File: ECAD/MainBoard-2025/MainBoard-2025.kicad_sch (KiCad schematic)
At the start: 60 parts, among them J1 XT60, J10 Conn_01x02, J11 Conn_01x04, J12 Conn_01x04, J15 Conn_01x02, J16 XT30, J17 XT30, J18 Conn_01x02, J2 Conn_01x04, J20 BAU, J21 BAU, J22 Conn_01x04, J23 Conn_01x02, J26 BAU, J28 Conn_01x02, J29 Conn_01x02, J3 ConStep1, J4 Conn_01x02, J5 ConStep1, J6 ConStep1, J7 XT30, J8 Conn_01x02, J9 Conn_01x02, K2 FINDER-36.11, U2 R-78B3.3-2.0, U3 R-78B12-2.0, U4 R-78B5.0-2.0, U5 Teensy4.1

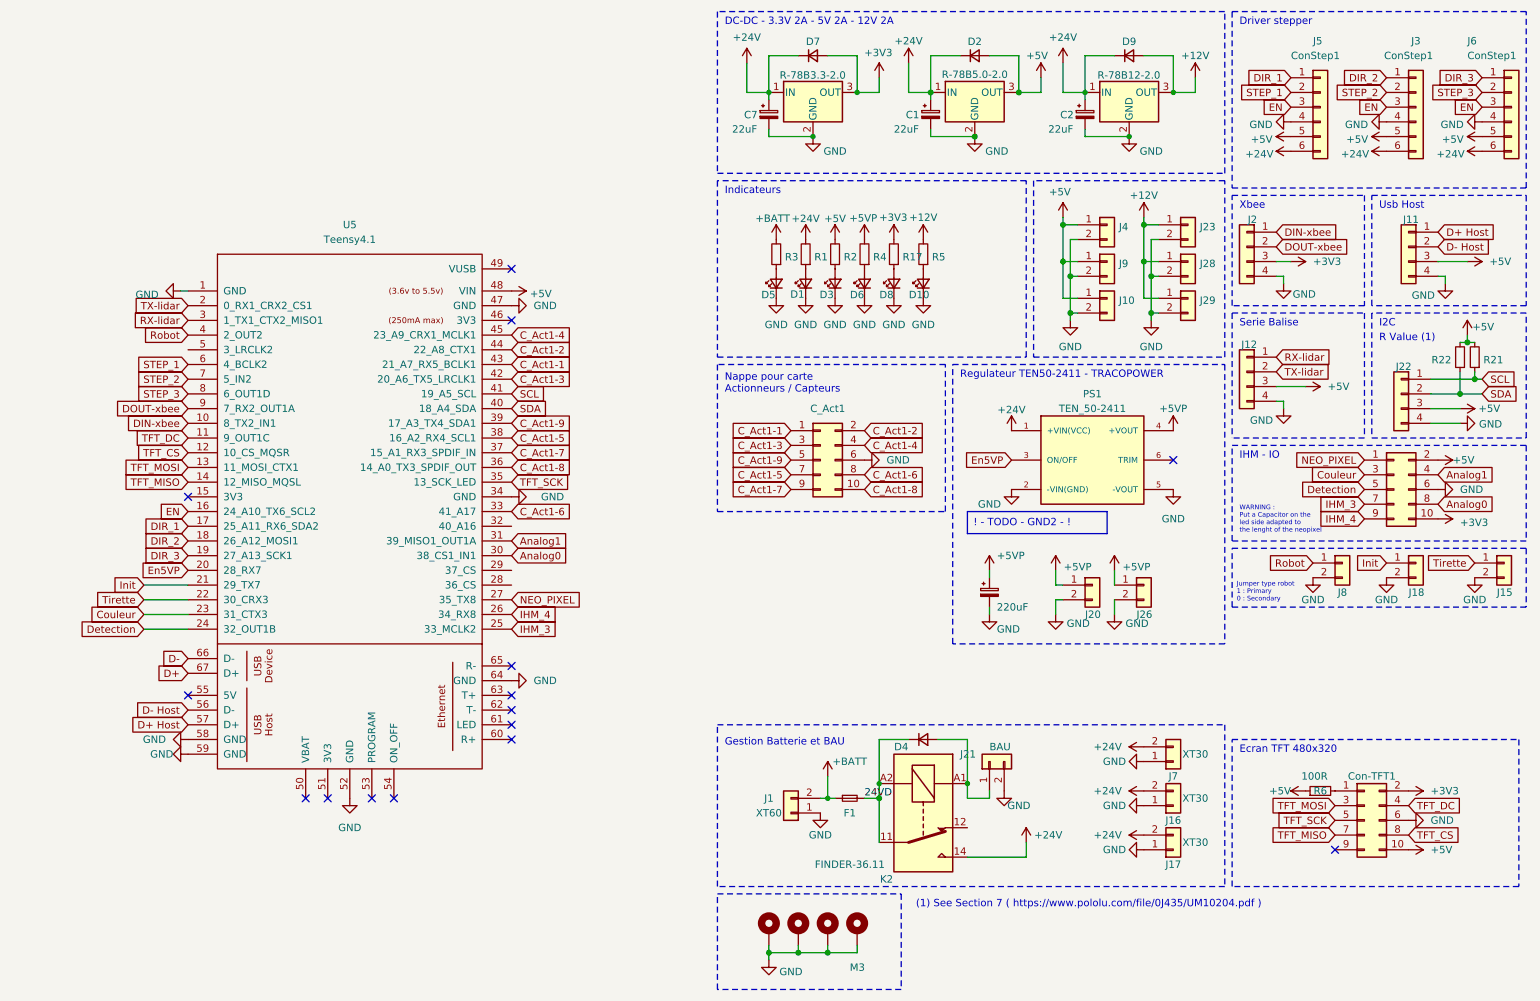
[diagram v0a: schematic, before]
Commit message: add buzzer and res on program
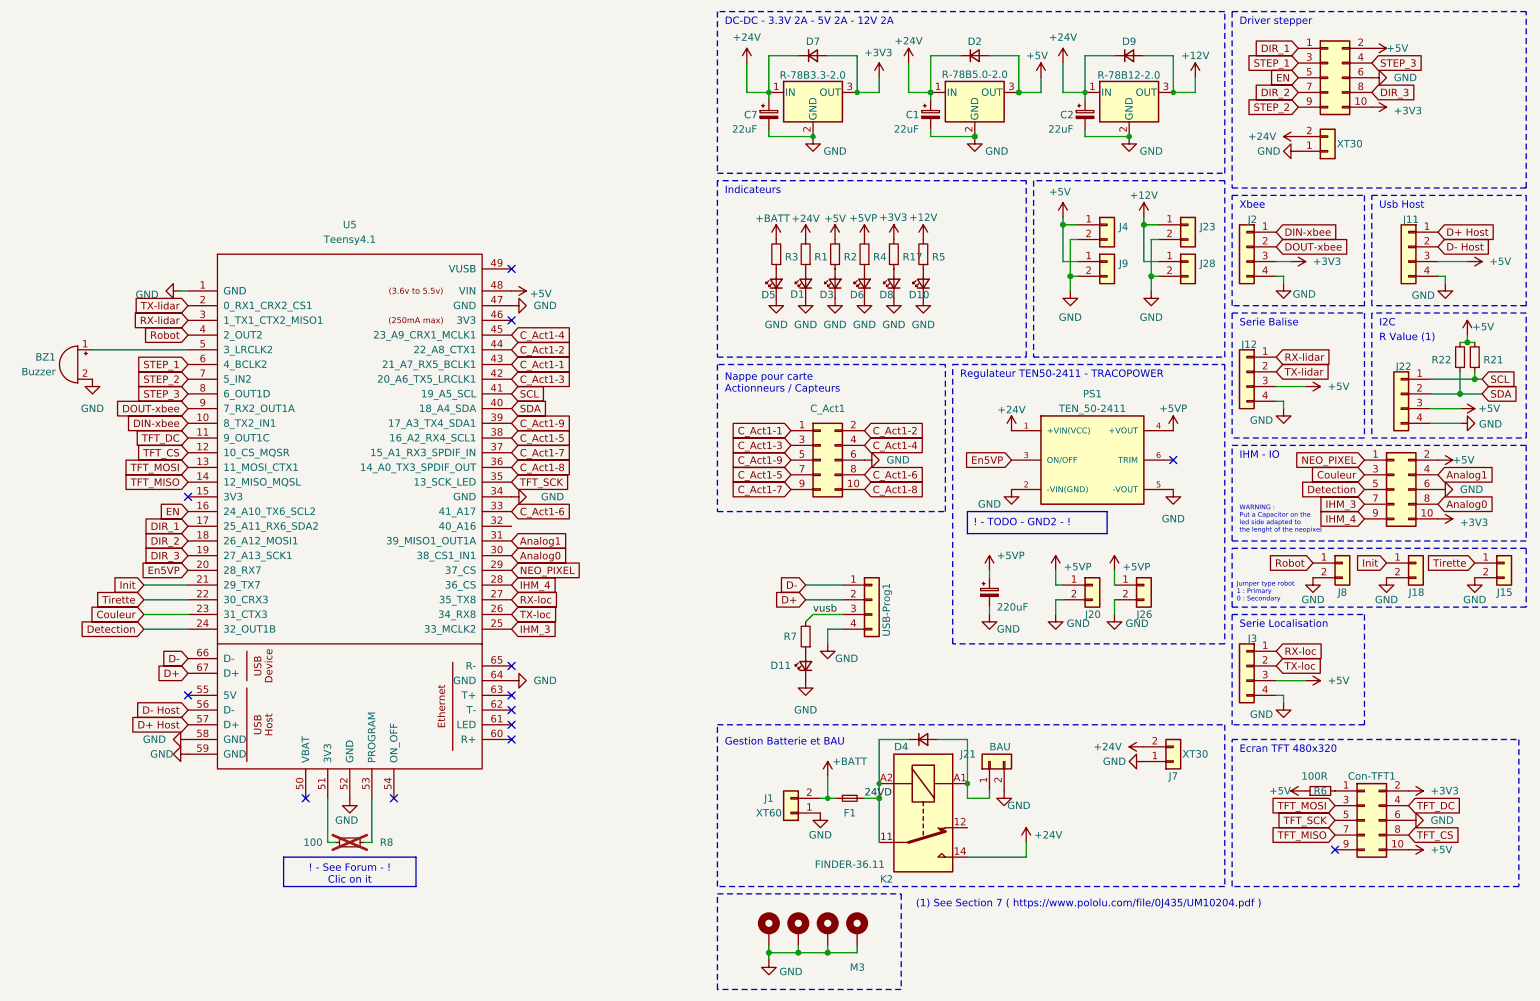
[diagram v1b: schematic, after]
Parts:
- removed J10, J29: Conn_01x02, Connector_Molex:Molex_KK-254_AE-6410-02A_1x02_P2.54mm_Vertical, symbol Connector_Generic:Conn_01x02
- removed J17: XT30, Connector_AMASS:AMASS_XT30U-F_1x02_P5.0mm_Vertical, symbol Connector_Generic:Conn_01x02
- removed J3, J5, J6: ConStep1, Connector_Molex:Molex_KK-254_AE-6410-06A_1x06_P2.54mm_Vertical, symbol Connector_Generic:Conn_01x06
- added BZ1: Buzzer, symbol Device:Buzzer
- added D11: LED_Small, LED_SMD:LED_1206_3216Metric_Pad1.42x1.75mm_HandSolder, symbol Device:LED_Small
- added IHM-IO2: Conn_02x05_Odd_Even, Connector_IDC:IDC-Header_2x05_P2.54mm_Vertical, symbol Connector_Generic:Conn_02x05_Odd_Even
- added J3, USB-Prog1: Conn_01x04, Connector_Molex:Molex_KK-254_AE-6410-04A_1x04_P2.54mm_Vertical, symbol Connector_Generic:Conn_01x04
- added R7: R_Small, Resistor_SMD:R_1206_3216Metric_Pad1.30x1.75mm_HandSolder, symbol Device:R_Small
- added R8: 100, Resistor_SMD:R_1206_3216Metric_Pad1.30x1.75mm_HandSolder, symbol Device:R_Small
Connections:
- net +3V3: now also IHM-IO2.10 (Pin_10)
- net +5V: now also IHM-IO2.2 (Pin_2), J3.3 (Pin_3)
- net D+: now also USB-Prog1.2 (Pin_2)
- net D-: now also USB-Prog1.1 (Pin_1)
- net DIR_1: now also IHM-IO2.1 (Pin_1)
- net DIR_2: now also IHM-IO2.7 (Pin_7)
- net DIR_3: now also IHM-IO2.8 (Pin_8)
- net EN: now also IHM-IO2.5 (Pin_5)
- net GND: now also BZ1.2 (-), D11.1 (K), IHM-IO2.6 (Pin_6), J3.4 (Pin_4), USB-Prog1.4 (Pin_4)
- net IHM_4: now also U5.28 (36_CS); no longer U5.26 (34_RX8)
- net NEO_PIXEL: now also U5.29 (37_CS); no longer U5.27 (35_TX8)
- net STEP_1: now also IHM-IO2.3 (Pin_3)
- net STEP_2: now also IHM-IO2.9 (Pin_9)
- net STEP_3: now also IHM-IO2.4 (Pin_4)
- net at U5.5 (3_LRCLK2): now also BZ1.1 (+)
- net at U5.51 (3V3): now also R8.2
- net at U5.53 (PROGRAM): now also R8.1
- new net: D11.2 (A), R7.1
- new net RX-loc: J3.1 (Pin_1), U5.27 (35_TX8)
- new net TX-loc: J3.2 (Pin_2), U5.26 (34_RX8)
- new net vusb: R7.2, USB-Prog1.3 (Pin_3)
- no-connect marks 15 -> 13
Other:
- note added: "Serie Localisation"
